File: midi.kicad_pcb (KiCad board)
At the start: 2 copper layers, 100 x 100 mm, 36 parts, among them J1 DIN-5_180degree, M1 MIDI IN, P1 Conn_01x02_Pin, SW1 SW_DIP_x01, SW2 SW_DIP_x01, SW3 SW_DIP_x01, SW4 SW_DIP_x01, SW5 SW_DIP_x01, U1 ESP32-DEVKITC-32D

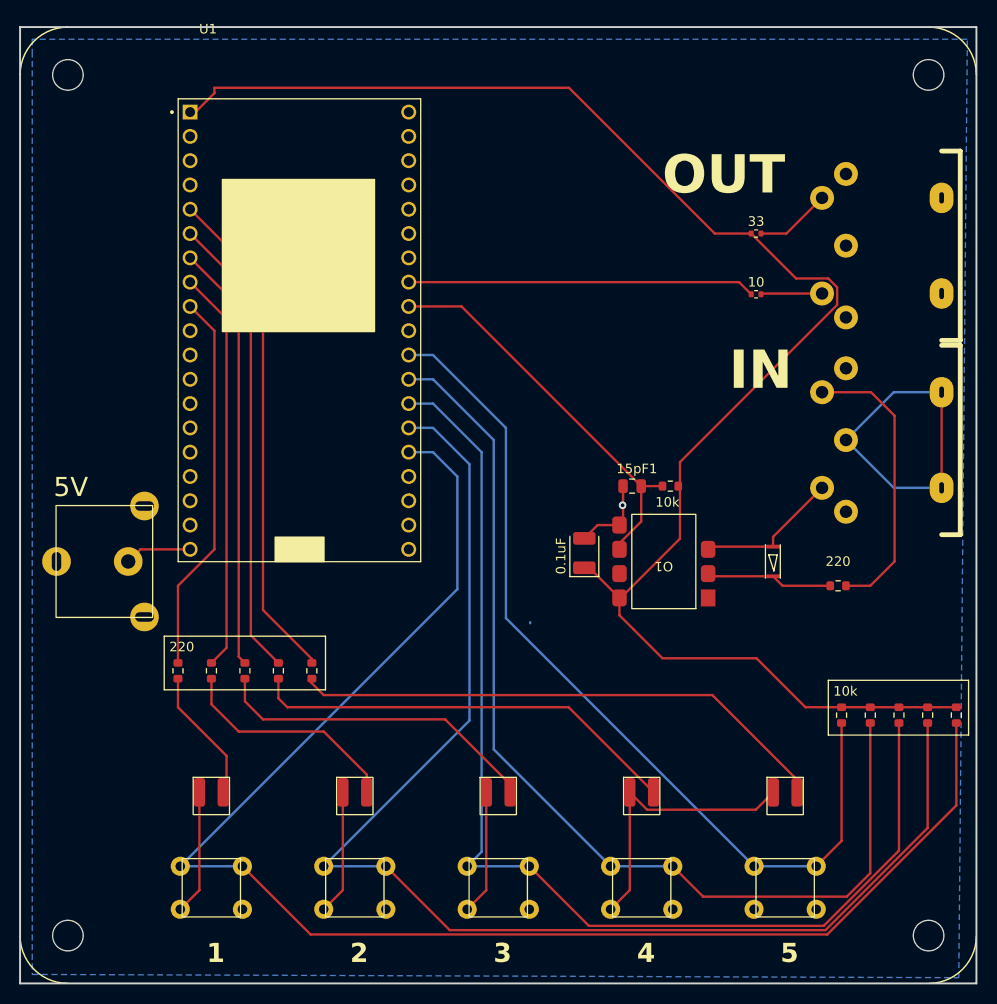
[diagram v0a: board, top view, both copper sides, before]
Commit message: update used pins
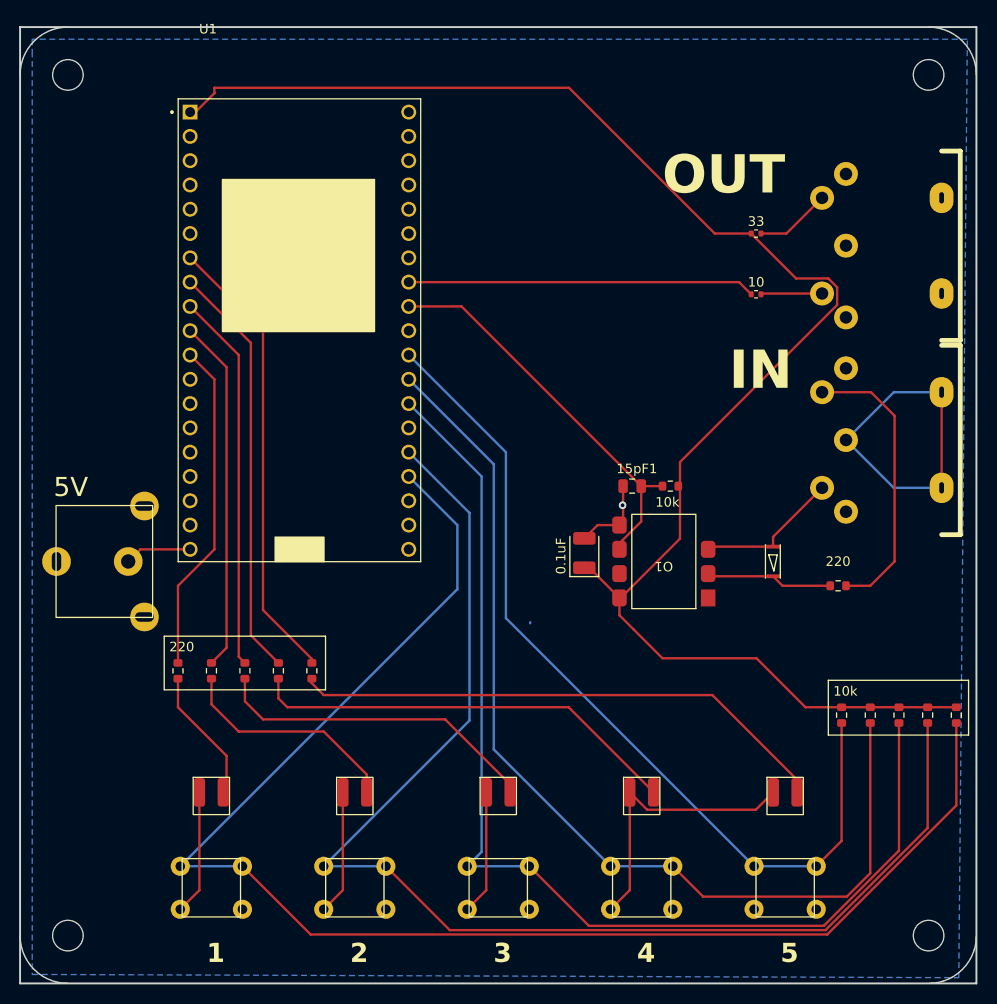
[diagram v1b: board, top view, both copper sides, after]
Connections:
- U1 pad J2-10: unconnected-(U1-IO26-PadJ2-10) -> LED2
- U1 pad J2-11: unconnected-(U1-IO27-PadJ2-11) -> LED1
- U1 pad J2-5: LED5 -> unconnected-(U1-IO34-PadJ2-5)
- U1 pad J2-6: LED4 -> unconnected-(U1-IO35-PadJ2-6)
- U1 pad J2-7: LED3 -> LED5
- U1 pad J2-8: LED2 -> LED4
- U1 pad J2-9: LED1 -> LED3
- U1 pad J3-14: SW2 -> unconnected-(U1-IO0-PadJ3-14)
- U1 pad J3-15: SW1 -> SW2
- U1 pad J3-16: unconnected-(U1-IO15-PadJ3-16) -> SW1
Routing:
- net LED5: track 52.7 -> 47.6 mm
- net LED4: track 48.7 -> 43.6 mm
- net LED3: track 44.7 -> 39.6 mm
- net LED1: track 39.9 -> 34.8 mm
- net LED2: track 42.0 -> 37.0 mm
- net SW2: track 137.6 -> 133.6 mm
- net SW1: track 157.2 -> 153.2 mm
- net SW3: track 118.0 -> 116.5 mm
- net SW5: track 92.5 -> 91.0 mm
- net SW4: track 106.3 -> 104.8 mm
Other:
- outline, holes or cut-outs redrawn
